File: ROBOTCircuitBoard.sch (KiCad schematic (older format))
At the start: 36 parts, among them J1 DB15_HighDensity_MountingHoles, J2 DB15_HighDensity_MountingHoles, P1 CONN_01X03, P2 CONN_01X04, P5 CONN_01X05, U1 MCP2551-I/P

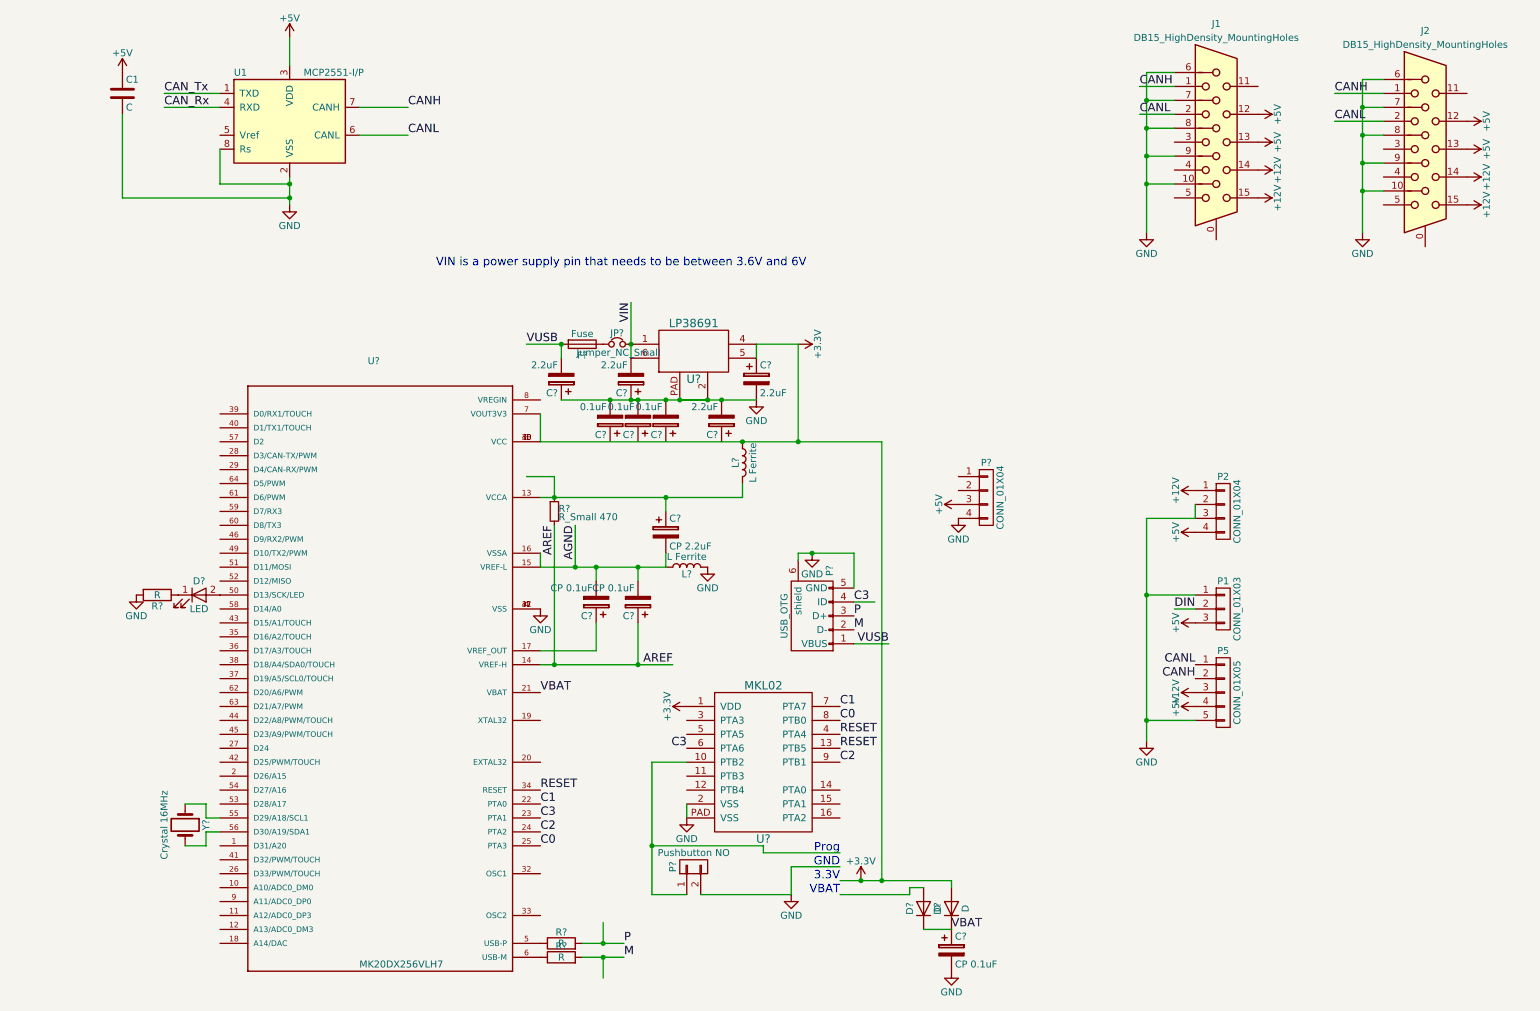
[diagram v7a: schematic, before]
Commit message: Began annotations and added dual shottkey Began annotation of schematic Added a two inpput one output shottkey diode instead of two diodes going to VBUS
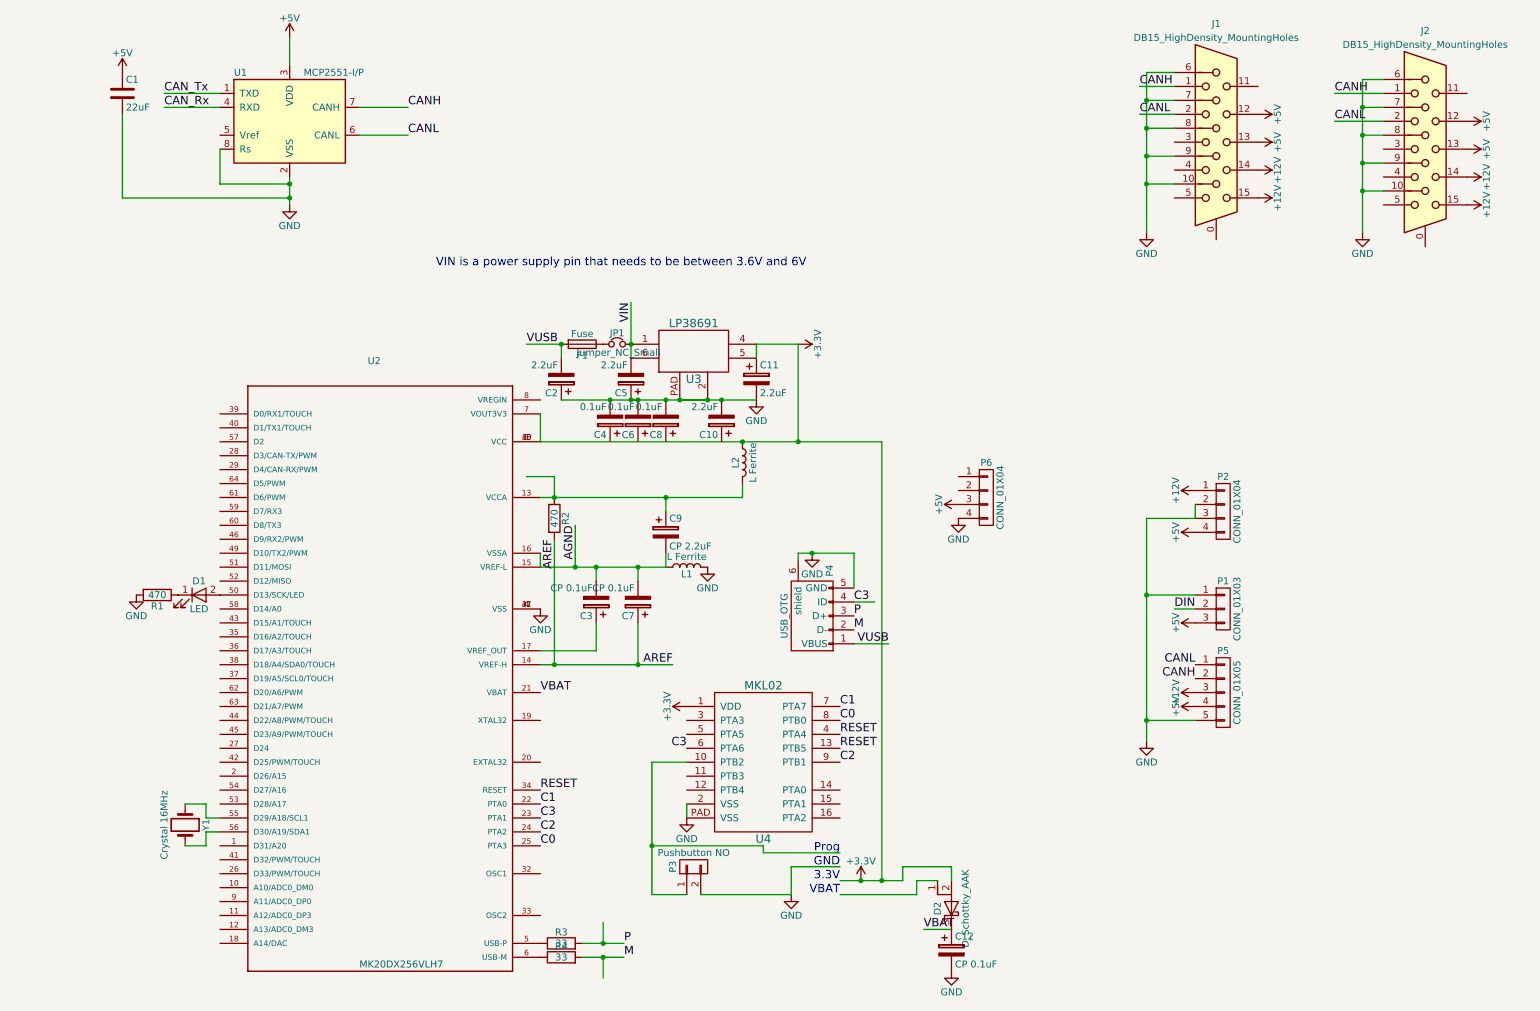
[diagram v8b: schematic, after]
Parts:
- removed D? (x2): D, symbol D
- removed R?: R_Small 470, symbol R_Small
- added D2: D_Schottky_AAK, Diodes_SMD:D_SOT-23_ANK, symbol D_Schottky_AAK
- added R2: 470, symbol R
- C1: value C -> 22uF; footprint Capacitors_SMD:C_0805 -> Capacitors_SMD:C_1210
- C10, C11, C2, C5, C9: renamed from C?; footprint (none) -> Capacitors_SMD:C_0805
- C12, C3, C4, C6, C7, C8: renamed from C?; footprint (none) -> Capacitors_SMD:C_0603
- F1: renamed from F?; footprint (none) -> Fuse_Holders_and_Fuses:Fuse_SMD1206_Reflow
- P4: renamed from P?; footprint (none) -> Connectors:USB_Micro-B
- P5: footprint Connectors_Terminal_Blocks:TerminalBlock_Pheonix_PT-3.5mm_5pol -> Pin_Headers:Pin_Header_Straight_1x05_Pitch2.54mm
- P6: renamed from P?; footprint (none) -> Pin_Headers:Pin_Header_Straight_1x04_Pitch2.54mm
- R1: renamed from R?; value R -> 470
- R3, R4: renamed from R?; value R -> 33
- gave numbers to parts that had none: 9
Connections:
- wire segments 91 -> 93
